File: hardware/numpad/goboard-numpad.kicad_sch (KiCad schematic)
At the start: 2 parts

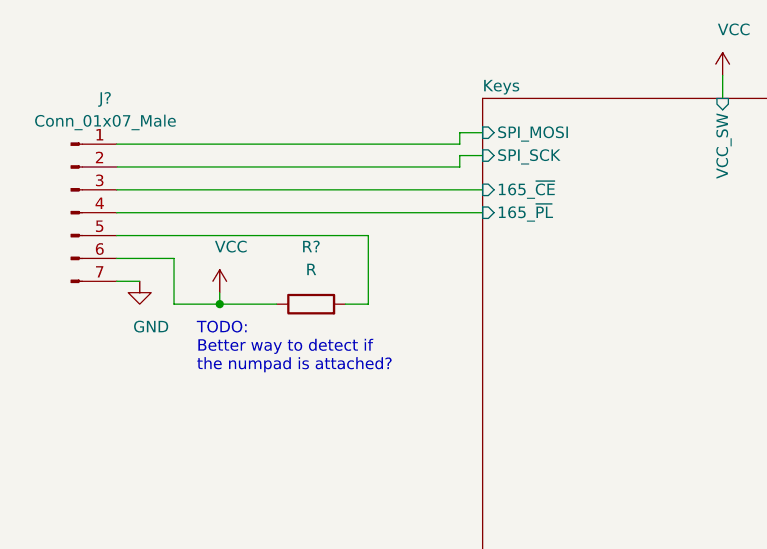
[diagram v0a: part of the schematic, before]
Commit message: Add the missing MISO to the connector
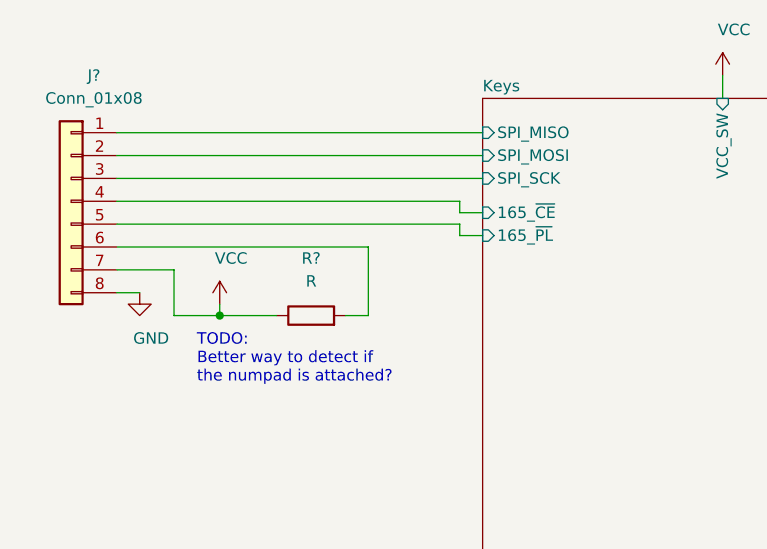
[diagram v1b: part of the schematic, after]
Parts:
- removed J?: Conn_01x07_Male, symbol Connector:Conn_01x07_Male
- added J?: Conn_01x08, symbol Connector_Generic:Conn_01x08
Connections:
- net GND: now also J?.8 (Pin_8)
- net Keys/165_~CE: now also J?.4 (Pin_4)
- net Keys/165_~PL: now also J?.5 (Pin_5)
- net Keys/SPI_MOSI: now also J?.2 (Pin_2)
- net Keys/SPI_SCK: now also J?.3 (Pin_3)
- net VCC: now also J?.7 (Pin_7)
- net at R?.2: now also J?.6 (Pin_6)
- new net Keys/SPI_MISO: J?.1 (Pin_1)
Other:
- sheet Keys ports: added SPI_MISO; removed none
- moved on the sheet: R?
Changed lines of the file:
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@@
 (kicad_sch (version 20201015) (generator eeschema)
   (paper "A4")
-  (junction (at 165.1 46.99) (diameter 0.9144) (color 0 0 0 0))
-  (wire (pts (xy 153.67 29.21) (xy 191.77 29.21))
+  (junction (at 165.1 48.26) (diameter 0.9144) (color 0 0 0 0))
+  (wire (pts (xy 153.67 27.94) (xy 194.31 27.94))
     (stroke (width 0) (type solid) (color 0 0 0 0))
   )
-  (wire (pts (xy 153.67 34.29) (xy 194.31 34.29))
+  (wire (pts (xy 153.67 30.48) (xy 194.31 30.48))
     (stroke (width 0) (type solid) (color 0 0 0 0))
   )
-  (wire (pts (xy 153.67 36.83) (xy 194.31 36.83))
+  (wire (pts (xy 153.67 33.02) (xy 194.31 33.02))
     (stroke (width 0) (type solid) (color 0 0 0 0))
   )
-  (wire (pts (xy 153.67 39.37) (xy 181.61 39.37))
+  (wire (pts (xy 153.67 35.56) (xy 191.77 35.56))
     (stroke (width 0) (type solid) (color 0 0 0 0))
   )
-  (wire (pts (xy 153.67 44.45) (xy 156.21 44.45))
+  (wire (pts (xy 153.67 38.1) (xy 191.77 38.1))
     (stroke (width 0) (type solid) (color 0 0 0 0))
   )
-  (wire (pts (xy 160.02 41.91) (xy 153.67 41.91))
+  (wire (pts (xy 153.67 40.64) (xy 181.61 40.64))
     (stroke (width 0) (type solid) (color 0 0 0 0))
   )
-  (wire (pts (xy 160.02 41.91) (xy 160.02 46.99))
+  (wire (pts (xy 153.67 45.72) (xy 156.21 45.72))
     (stroke (width 0) (type solid) (color 0 0 0 0))
   )
-  (wire (pts (xy 165.1 45.72) (xy 165.1 46.99))
+  (wire (pts (xy 160.02 43.18) (xy 153.67 43.18))
     (stroke (width 0) (type solid) (color 0 0 0 0))
   )
-  (wire (pts (xy 165.1 46.99) (xy 160.02 46.99))
+  (wire (pts (xy 160.02 43.18) (xy 160.02 48.26))
     (stroke (width 0) (type solid) (color 0 0 0 0))
   )
-  (wire (pts (xy 171.45 46.99) (xy 165.1 46.99))
+  (wire (pts (xy 165.1 46.99) (xy 165.1 48.26))
     (stroke (width 0) (type solid) (color 0 0 0 0))
   )
-  (wire (pts (xy 181.61 39.37) (xy 181.61 46.99))
+  (wire (pts (xy 165.1 48.26) (xy 160.02 48.26))
     (stroke (width 0) (type solid) (color 0 0 0 0))
   )
-  (wire (pts (xy 181.61 46.99) (xy 179.07 46.99))
+  (wire (pts (xy 171.45 48.26) (xy 165.1 48.26))
     (stroke (width 0) (type solid) (color 0 0 0 0))
   )
-  (wire (pts (xy 191.77 27.94) (xy 194.31 27.94))
+  (wire (pts (xy 181.61 40.64) (xy 181.61 48.26))
     (stroke (width 0) (type solid) (color 0 0 0 0))
   )
-  (wire (pts (xy 191.77 29.21) (xy 191.77 27.94))
+  (wire (pts (xy 181.61 48.26) (xy 179.07 48.26))
     (stroke (width 0) (type solid) (color 0 0 0 0))
   )
-  (wire (pts (xy 191.77 30.48) (xy 191.77 31.75))
+  (wire (pts (xy 191.77 35.56) (xy 191.77 36.83))
     (stroke (width 0) (type solid) (color 0 0 0 0))
   )
-  (wire (pts (xy 191.77 31.75) (xy 153.67 31.75))
+  (wire (pts (xy 191.77 36.83) (xy 194.31 36.83))
     (stroke (width 0) (type solid) (color 0 0 0 0))
   )
-  (wire (pts (xy 194.31 30.48) (xy 191.77 30.48))
+  (wire (pts (xy 191.77 39.37) (xy 191.77 38.1))
+    (stroke (width 0) (type solid) (color 0 0 0 0))
+  )
+  (wire (pts (xy 194.31 39.37) (xy 191.77 39.37))
     (stroke (width 0) (type solid) (color 0 0 0 0))
   )
@@
   )
   (text "TODO:\nBetter way to detect if\nthe numpad is attached?"
-    (at 162.56 54.61 0)
+    (at 162.56 55.88 0)
     (effects (font (size 1.27 1.27)) (justify left bottom))
   )
-  (symbol (lib_id "power:VCC") (at 165.1 45.72 0) (unit 1)
+  (symbol (lib_id "power:VCC") (at 165.1 46.99 0) (unit 1)
     (in_bom yes) (on_board yes)
-    (property "Reference" "#PWR?" (id 0) (at 165.1 49.53 0)
+    (property "Reference" "#PWR?" (id 0) (at 165.1 50.8 0)
       (effects (font (size 1.27 1.27)) hide)
     )
-    (property "Value" "VCC" (id 1) (at 166.37 40.64 0))
-    (property "Footprint" "" (id 2) (at 165.1 45.72 0)
+    (property "Value" "VCC" (id 1) (at 166.37 41.91 0))
+    (property "Footprint" "" (id 2) (at 165.1 46.99 0)
       (effects (font (size 1.27 1.27)) hide)
     )
-    (property "Datasheet" "" (id 3) (at 165.1 45.72 0)
+    (property "Datasheet" "" (id 3) (at 165.1 46.99 0)
       (effects (font (size 1.27 1.27)) hide)
     )
@@
     )
   )
-  (symbol (lib_id "power:GND") (at 156.21 44.45 0) (unit 1)
+  (symbol (lib_id "power:GND") (at 156.21 45.72 0) (unit 1)
     (in_bom yes) (on_board yes)
-    (property "Reference" "#PWR?" (id 0) (at 156.21 50.8 0)
+    (property "Reference" "#PWR?" (id 0) (at 156.21 52.07 0)
       (effects (font (size 1.27 1.27)) hide)
     )
-    (property "Value" "GND" (id 1) (at 157.48 49.53 0))
-    (property "Footprint" "" (id 2) (at 156.21 44.45 0)
+    (property "Value" "GND" (id 1) (at 157.48 50.8 0))
+    (property "Footprint" "" (id 2) (at 156.21 45.72 0)
       (effects (font (size 1.27 1.27)) hide)
     )
-    (property "Datasheet" "" (id 3) (at 156.21 44.45 0)
+    (property "Datasheet" "" (id 3) (at 156.21 45.72 0)
       (effects (font (size 1.27 1.27)) hide)
     )
   )
-  (symbol (lib_id "Device:R") (at 175.26 46.99 90) (unit 1)
+  (symbol (lib_id "Device:R") (at 175.26 48.26 90) (unit 1)
     (in_bom yes) (on_board yes)
-    (property "Reference" "R?" (id 0) (at 175.26 40.64 90))
-    (property "Value" "R" (id 1) (at 175.26 43.18 90))
-    (property "Footprint" "" (id 2) (at 175.26 48.768 90)
+    (property "Reference" "R?" (id 0) (at 175.26 41.91 90))
+    (property "Value" "R" (id 1) (at 175.26 44.45 90))
+    (property "Footprint" "" (id 2) (at 175.26 50.038 90)
       (effects (font (size 1.27 1.27)) hide)
     )
-    (property "Datasheet" "~" (id 3) (at 175.26 46.99 0)
+    (property "Datasheet" "~" (id 3) (at 175.26 48.26 0)
       (effects (font (size 1.27 1.27)) hide)
     )
   )
-  (symbol (lib_id "Connector:Conn_01x07_Male") (at 148.59 36.83 0) (unit 1)
+  (symbol (lib_id "Connector_Generic:Conn_01x08") (at 148.59 35.56 0) (mirror y) (unit 1)
     (in_bom yes) (on_board yes)
-    (property "Reference" "J?" (id 0) (at 152.4 24.13 0))
-    (property "Value" "Conn_01x07_Male" (id 1) (at 152.4 26.67 0))
-    (property "Footprint" "" (id 2) (at 148.59 36.83 0)
+    (property "Reference" "J?" (id 0) (at 151.13 21.59 0))
+    (property "Value" "Conn_01x08" (id 1) (at 151.13 24.13 0))
+    (property "Footprint" "" (id 2) (at 148.59 35.56 0)
       (effects (font (size 1.27 1.27)) hide)
     )
-    (property "Datasheet" "~" (id 3) (at 148.59 36.83 0)
+    (property "Datasheet" "~" (id 3) (at 148.59 35.56 0)
       (effects (font (size 1.27 1.27)) hide)
     )
@@
       (effects (font (size 1.27 1.27)) (justify left top))
     )
-    (pin "SPI_SCK" input (at 194.31 30.48 180)
+    (pin "SPI_SCK" input (at 194.31 33.02 180)
       (effects (font (size 1.27 1.27)) (justify left))
     )
@@
       (effects (font (size 1.27 1.27)) (justify right))
     )
-    (pin "165_~CE" input (at 194.31 34.29 180)
+    (pin "165_~CE" input (at 194.31 36.83 180)
       (effects (font (size 1.27 1.27)) (justify left))
     )
-    (pin "165_~PL" input (at 194.31 36.83 180)
+    (pin "165_~PL" input (at 194.31 39.37 180)
       (effects (font (size 1.27 1.27)) (justify left))
     )
-    (pin "SPI_MOSI" input (at 194.31 27.94 180)
+    (pin "SPI_MOSI" input (at 194.31 30.48 180)
+      (effects (font (size 1.27 1.27)) (justify left))
+    )
+    (pin "SPI_MISO" input (at 194.31 27.94 180)
       (effects (font (size 1.27 1.27)) (justify left))
     )
@@
       (reference "#PWR?") (unit 1) (value "GND") (footprint "")
     )
-    (path "/b3892fa1-855b-4ccf-8cb0-c96043980b30"
-      (reference "J?") (unit 1) (value "Conn_01x07_Male") (footprint "")
+    (path "/adaff78d-862a-4d01-a5c2-f0465b5ce7be"
+      (reference "J?") (unit 1) (value "Conn_01x08") (footprint "")
     )
     (path "/b3b33e03-9b1f-42d4-b343-d85164fbeaec"

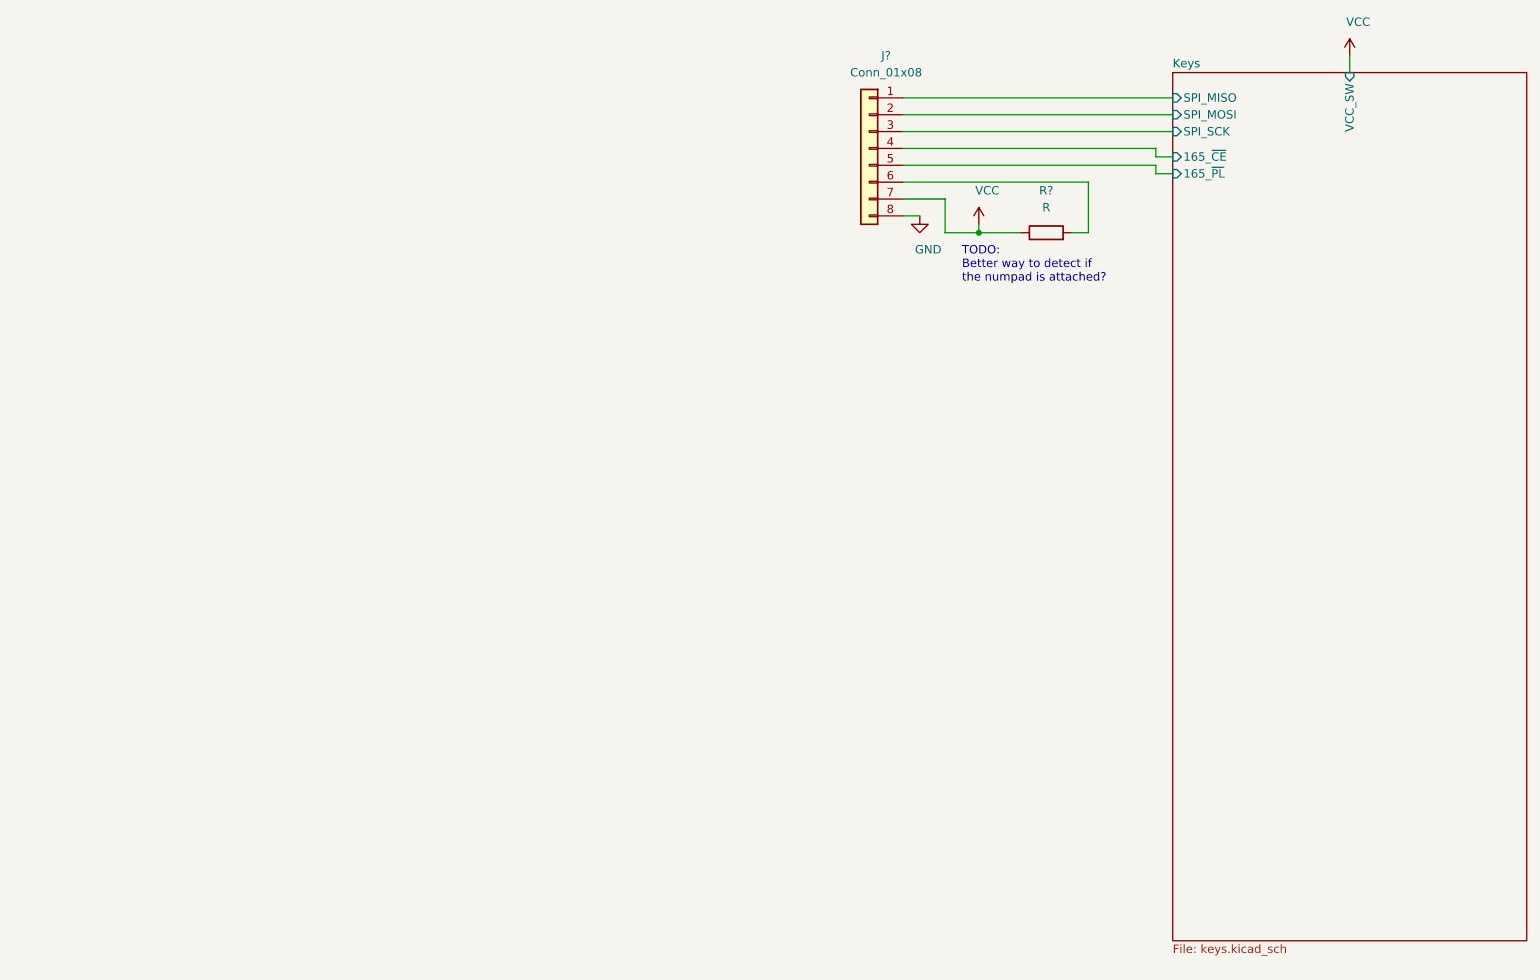
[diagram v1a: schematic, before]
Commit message: WIP: numpad with an ATtiny
As the newer versions of the ATtiny cannot be programmed using an
In-Circuit-Programmer based on SPI this variant is not pursued further.
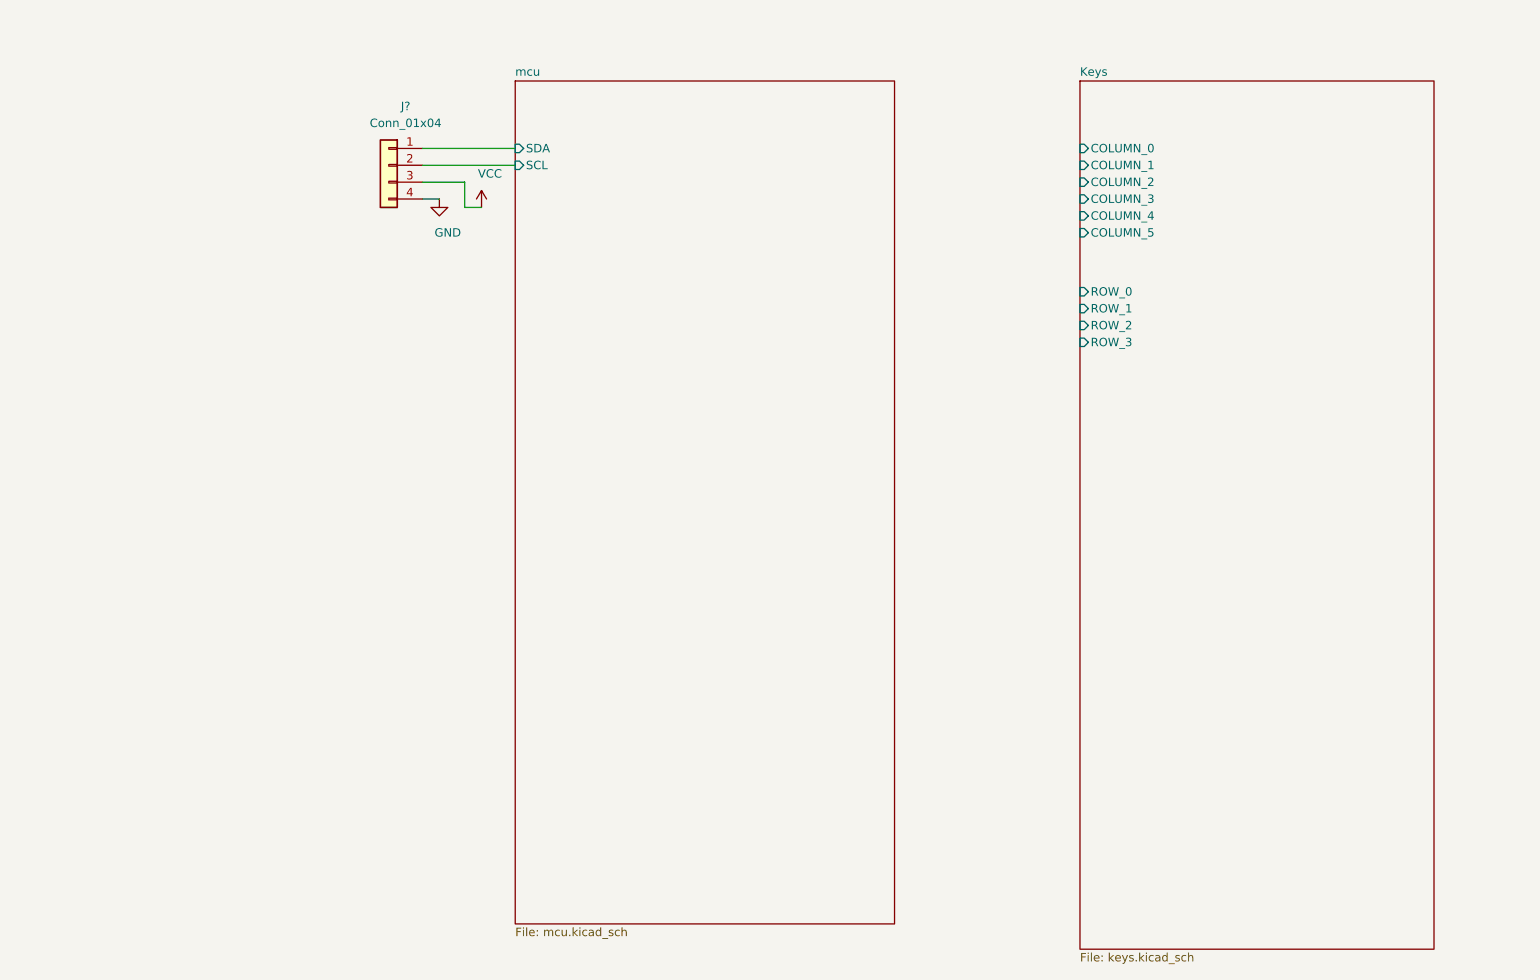
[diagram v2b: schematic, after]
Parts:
- removed J?: Conn_01x08, symbol Connector_Generic:Conn_01x08
- removed R?: R, symbol Device:R
- added J?: Conn_01x04, symbol Connector_Generic:Conn_01x04
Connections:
- net GND: now also J?.4 (Pin_4)
- net VCC: now also J?.3 (Pin_3)
- new net mcu/SCL: J?.2 (Pin_2)
- new net mcu/SDA: J?.1 (Pin_1)
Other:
- added sheet mcu (mcu.kicad_sch)
- sheet Keys ports: added COLUMN_0, COLUMN_1, COLUMN_2, COLUMN_3, COLUMN_4, COLUMN_5, ROW_0, ROW_1, ROW_2, ROW_3; removed 165_~CE, 165_~PL, SPI_MISO, SPI_MOSI, SPI_SCK, VCC_SW
- note removed: "TODO: Better way to detect if the numpad is attached?"

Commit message: Exchange the ATtiny with a STM32L011F4P6 for the numpad
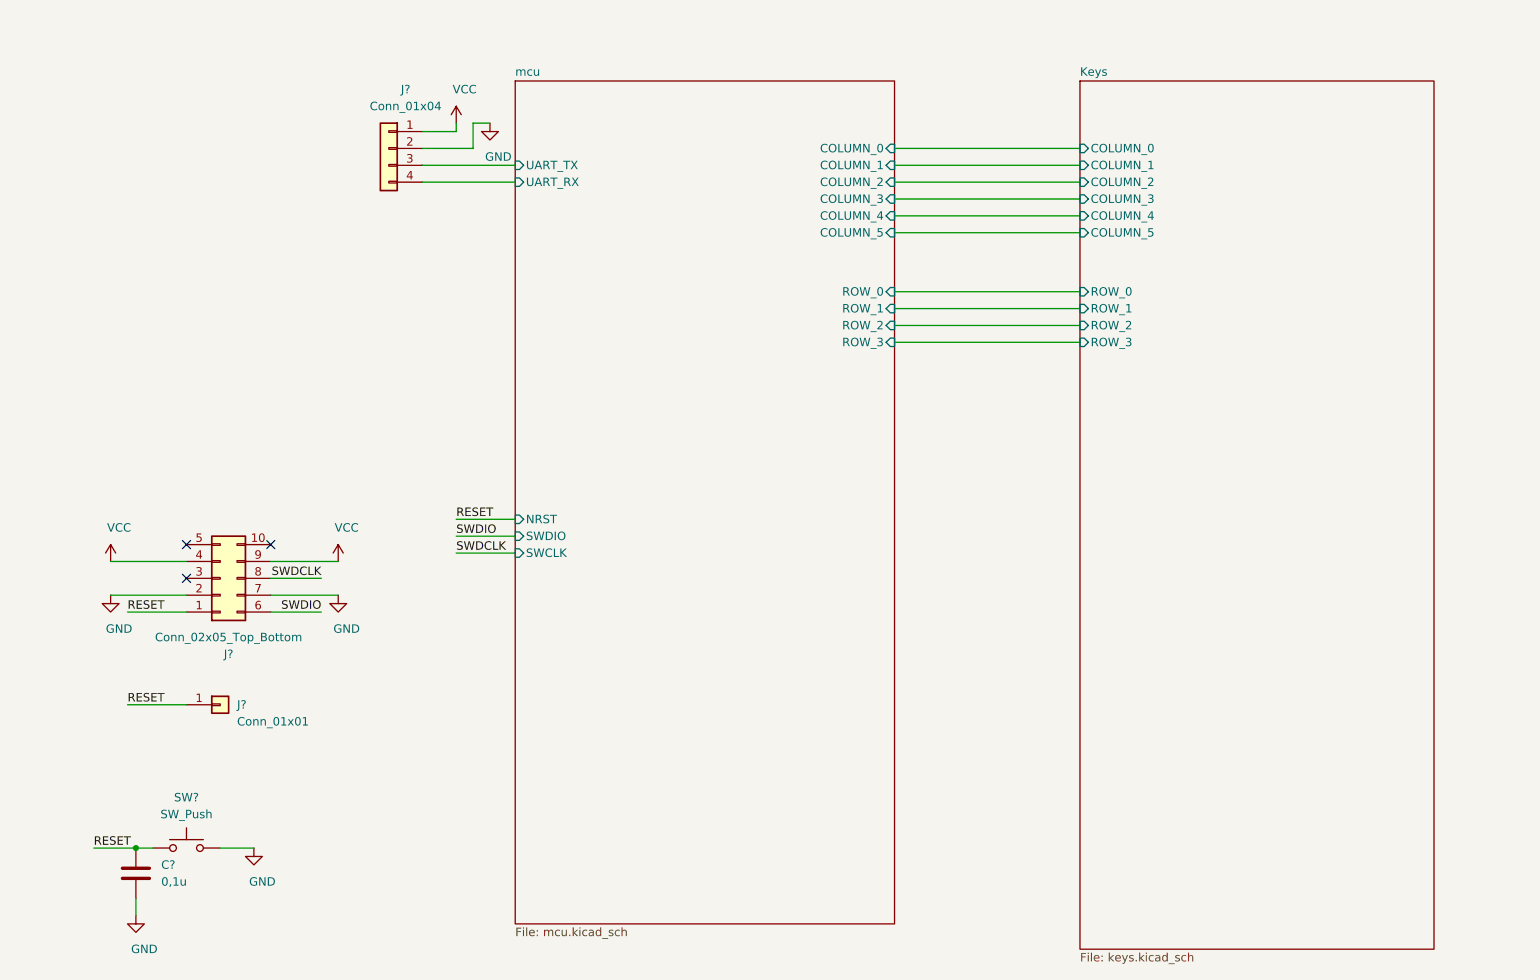
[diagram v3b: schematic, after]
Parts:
- removed J?: Conn_01x04, symbol Connector_Generic:Conn_01x04
- added C?: 0,1u, symbol Device:C
- added J?: Conn_02x05_Top_Bottom, symbol Connector_Generic:Conn_02x05_Top_Bottom
- added J?: Conn_01x04, symbol Connector_Generic:Conn_01x04
- added J?: Conn_01x01, symbol Connector_Generic:Conn_01x01
- added SW?: SW_Push, symbol Switch:SW_Push
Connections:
- net GND: now also C?.2, J?.2 (Pin_2), J?.2 (Pin_2), J?.7 (Pin_7), SW?.2
- net VCC: now also J?.1 (Pin_1), J?.4 (Pin_4), J?.9 (Pin_9)
- new net RESET: C?.1, J?.1 (Pin_1), J?.1 (Pin_1), SW?.1
- new net SWDCLK: J?.8 (Pin_8)
- new net SWDIO: J?.6 (Pin_6)
- new net mcu/UART_RX: J?.4 (Pin_4)
- new net mcu/UART_TX: J?.3 (Pin_3)
- no-connect marks 0 -> 3
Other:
- sheet mcu ports: added COLUMN_0, COLUMN_1, COLUMN_2, COLUMN_3, COLUMN_4, COLUMN_5, NRST, ROW_0, ROW_1, ROW_2, ROW_3, SWCLK, SWDIO, UART_RX, UART_TX; removed SCL, SDA
